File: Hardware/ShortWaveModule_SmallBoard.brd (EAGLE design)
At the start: 36.8 x 31.8 mm, 56 parts, among them J1 CONN_42.54_SCREW, J2 CONN_42.54, J3 CONN_42.54, J4 CONN_42.54, Q1 2N7002, Q2 2N7002, Q3 DMG3404, U1 ADXL343, U2 ATTINY441/841841, U3 LTC2050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

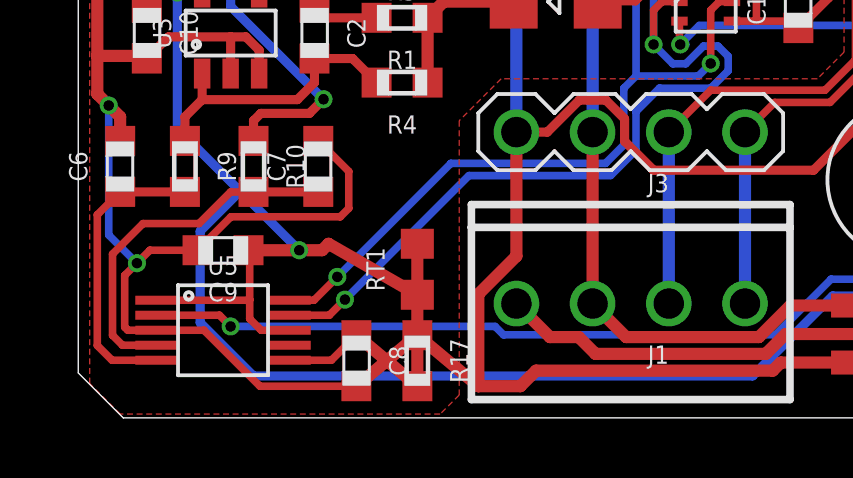
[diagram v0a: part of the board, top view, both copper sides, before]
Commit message: Generated gerbers for Mrk 0.1
Added Gerbers for Mrk 0.1 revision, fixed silk screen issues, added pullup resistors for on board I2C on shortwave module, and changed amplifiers on longwave module (eliminated use of LTC2054HV, and switched to using LTC2050HV due to availability), also fixed (flipped) thermistor arraignment on shortwave module
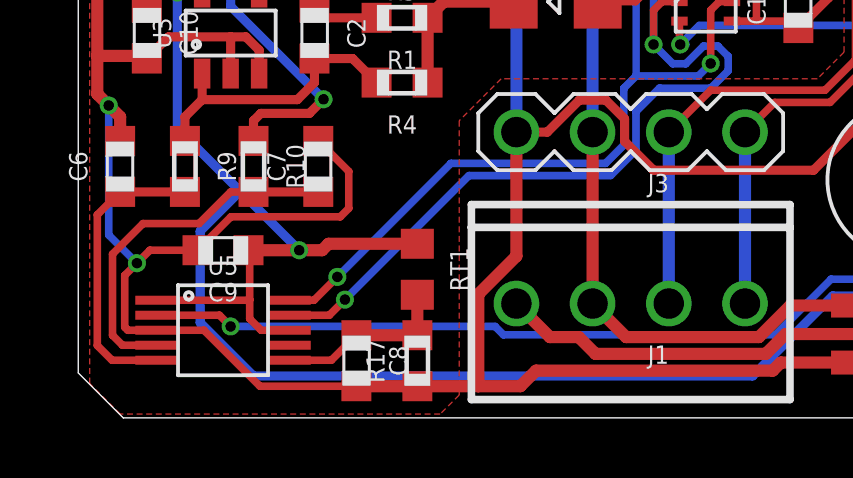
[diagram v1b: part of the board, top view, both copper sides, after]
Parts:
- JP1: value JUMPER-SMT_2_NC_PASTE_SILK -> JUMPER-SMT_2_NO_SILK; device SparkFun-Jumpers:SMT-JUMPER_2_NC_PASTE_SILK -> SparkFun-Jumpers:SMT-JUMPER_2_NO_SILK
- U3, U4: value LTC2050 -> LTC2054
- turned R17 to 90 degrees
- turned RT1 to 270 degrees
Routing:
- net AOUT_THERM: track 9.99 -> 5.97 mm
- net GND: track 181.4 -> 180.2 mm
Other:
- board text added: "Project Dyson v0.1 ShortWave ---------------- Developed by Northern Widget and University of Minnesota"
- board text added: "±"
- board text removed: "Project Dyson v0.0 ShortWave ---------------- Developed by Northern Widget and University of Minnesota"

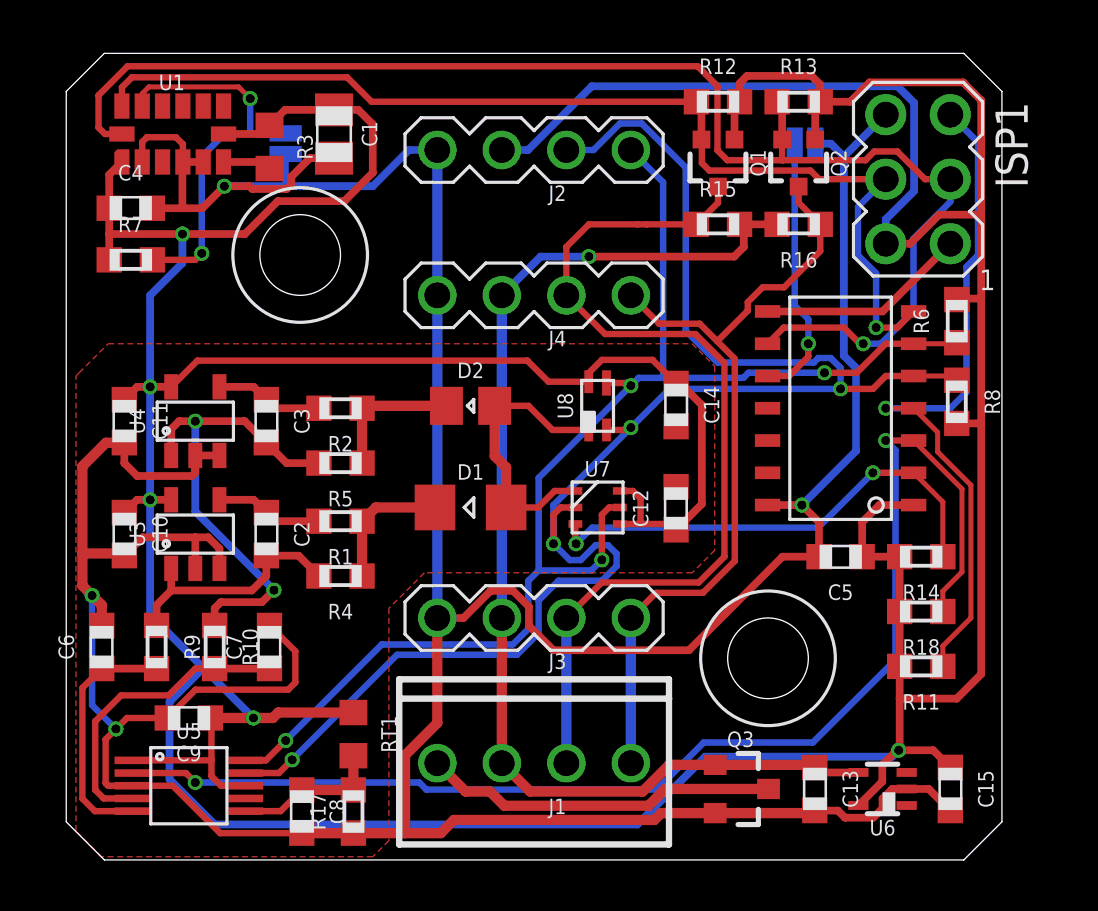
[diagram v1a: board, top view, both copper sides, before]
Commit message: Added mechanical parts and updated gerbers and ref designators
Updated gerbers for long wave and fixed reference designators for short wave
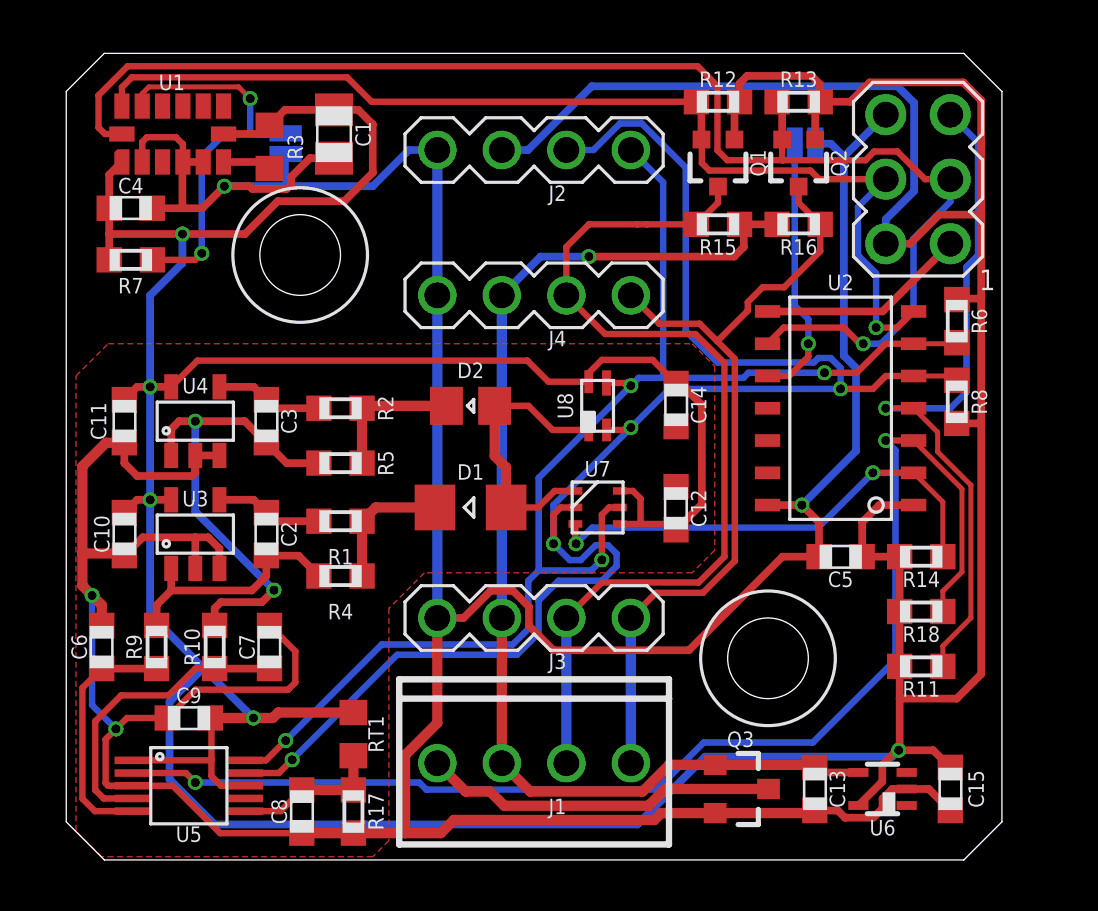
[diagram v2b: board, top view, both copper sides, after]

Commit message: Dyson --> Monarch in sch and on silk
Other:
- board text added: "Project Monarch v0.1 ShortWave ---------------- Developed by Northern Widget and University of Minnesota"
- board text removed: "Project Dyson v0.1 ShortWave ---------------- Developed by Northern Widget and University of Minnesota"
